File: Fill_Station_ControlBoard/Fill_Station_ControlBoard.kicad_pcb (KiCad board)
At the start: 6 copper layers, 100 x 100 mm, 251 parts, among them IC1 TPS259573DSGR, J1 RJ45_Wuerth_74980111211, J10 Micro_SD_Card_Det_Hirose_DM3AT, J12 Conn_02x05_Counter_Clockwise, J13 Screw_Terminal_2_P5.00mm, J14 Micro_SD_Card_Det_Hirose_DM3AT, J15 USB_C_Receptacle_USB2.0_14P, J16 DE9_Socket_MountingHoles, J18 Screw_Terminal_3_P3.50mm, J2 Ematch1, J6 Ematch2, J7 Screw_Terminal_3_P3.50mm, J8 Screw_Terminal_3_P3.50mm, J9 Screw_Terminal_6_P3.50mm, Q1 AO3400A, Q2 AO3400A, SW1 RESET, SW2 BOOT, U1 TPS62130, U2 STM32H747IITx, U3 INA3221, U4 TPS62130, U5 DP83825I, U6 TPS2116DRL, U7 USBLC6-2SC6, U8 ISOW1044, Y1 ASV-25.000MHz, Y2 ASV-32.768kHz, Y4 ASV-25.000MHz

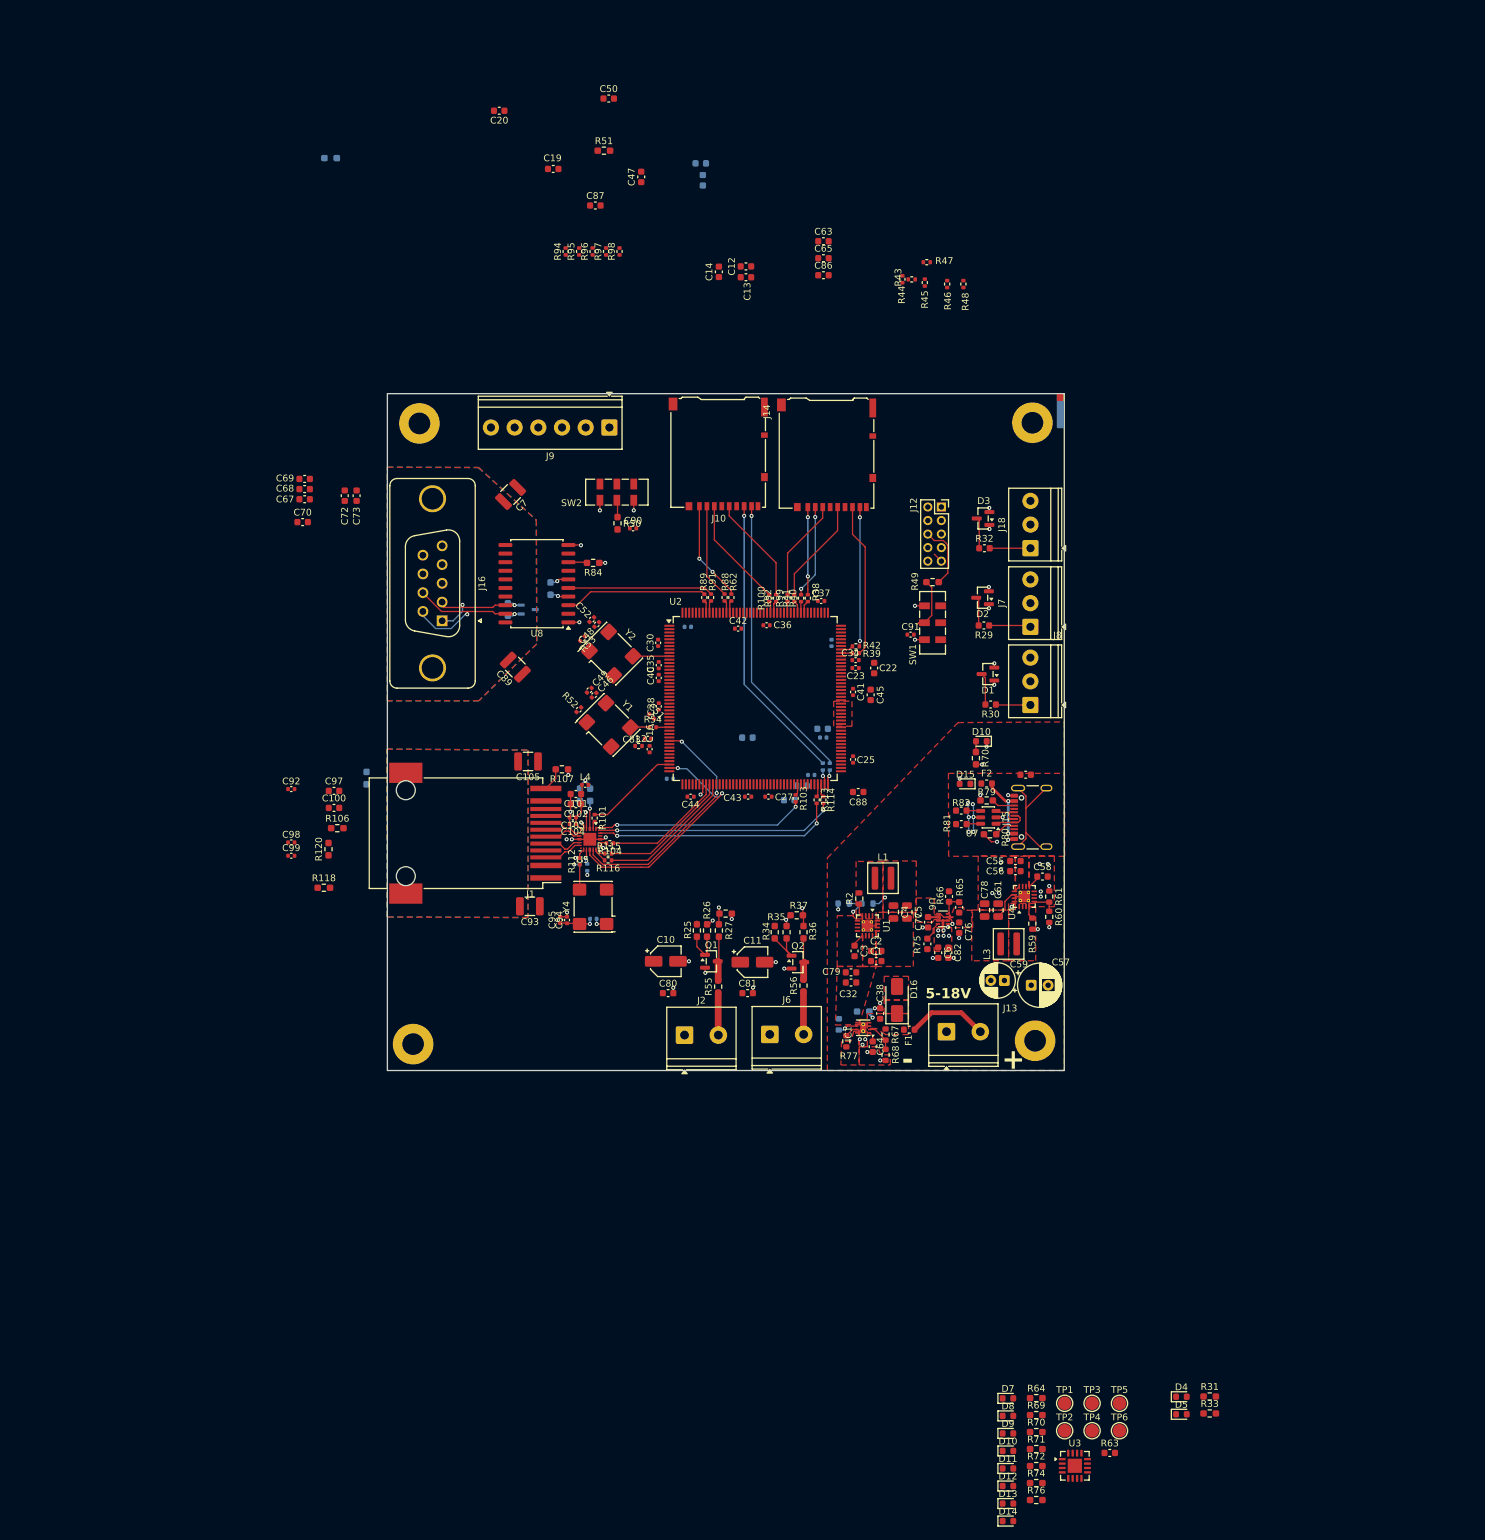
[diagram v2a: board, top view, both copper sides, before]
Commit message: PCB presque terminé
Modifs de l'alim
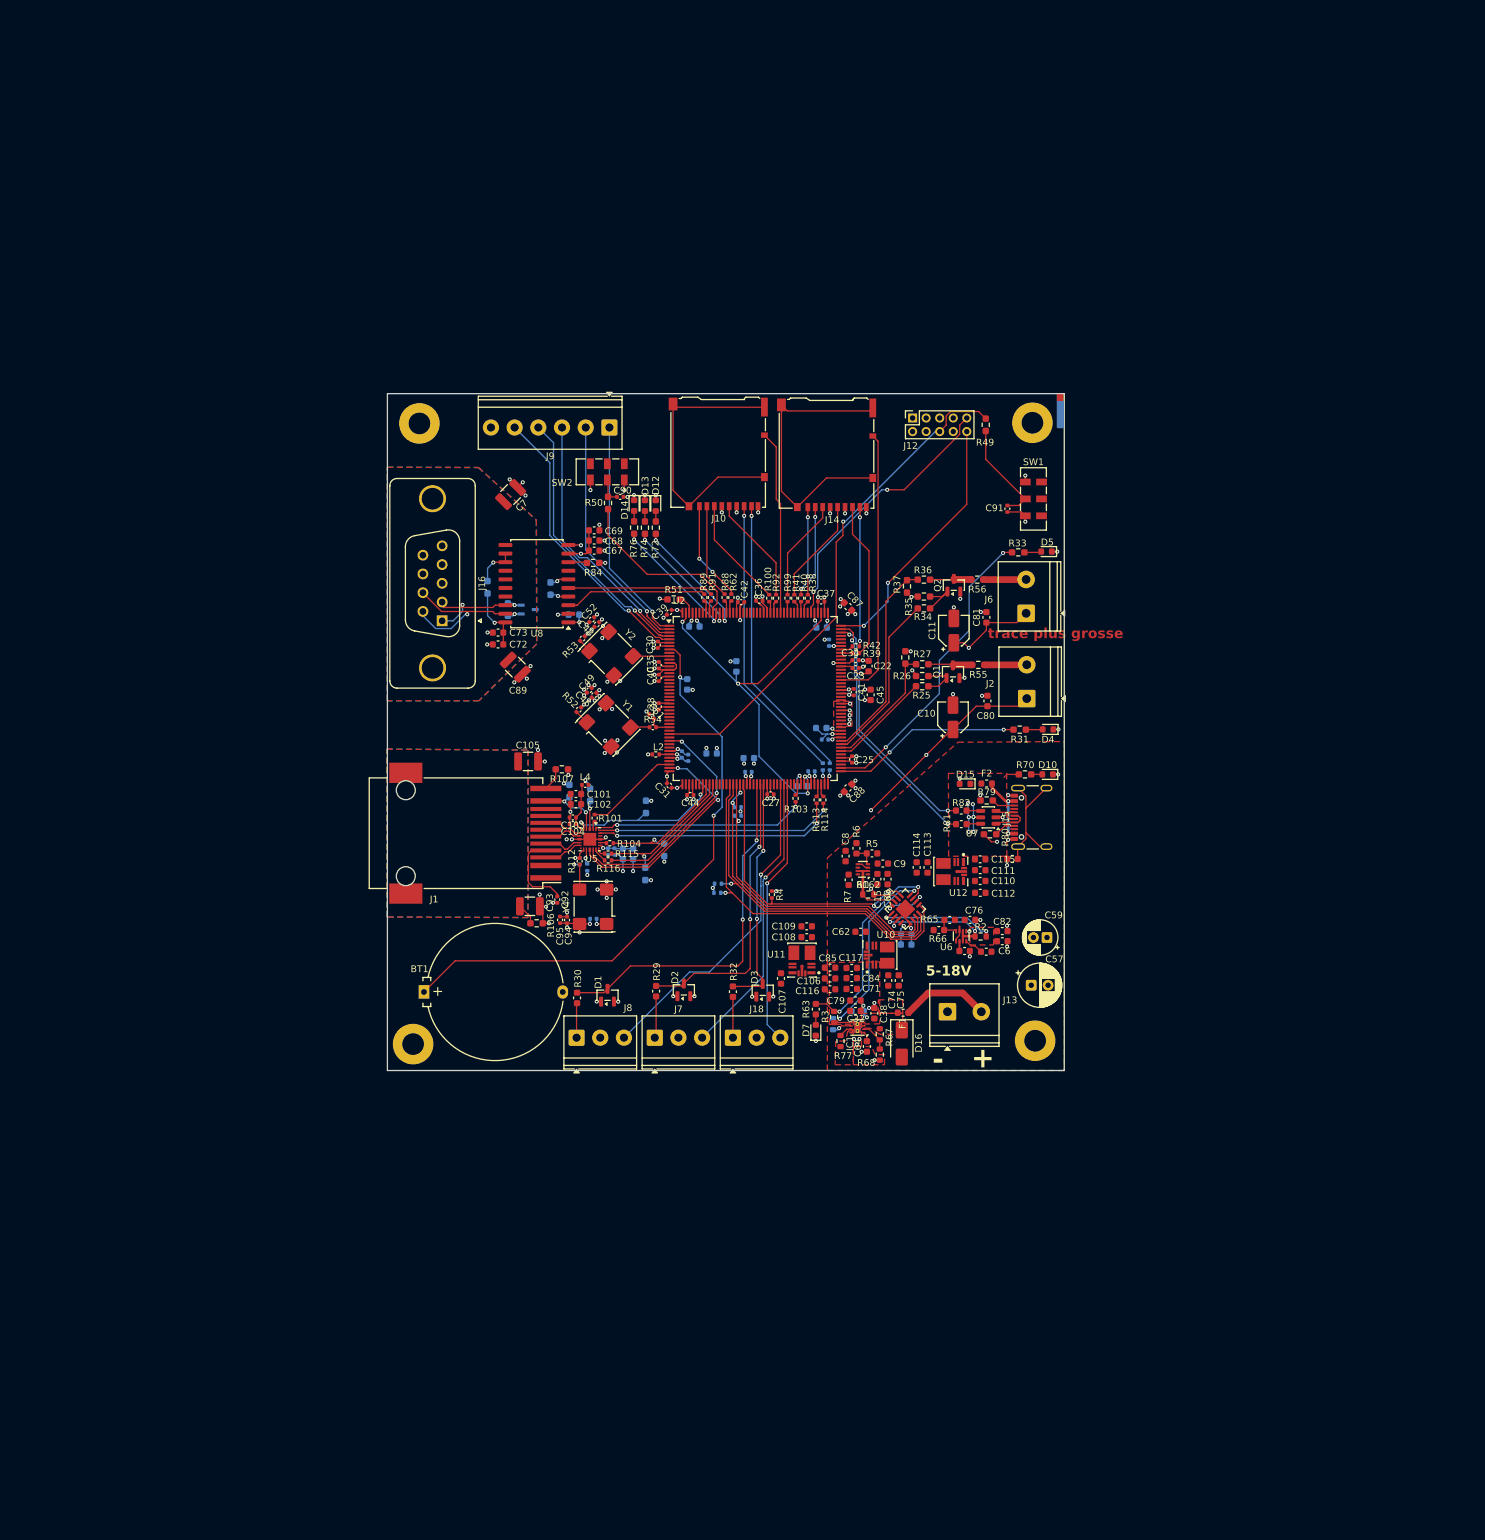
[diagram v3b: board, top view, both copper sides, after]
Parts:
- removed C12, C14, C63, C86: 100n, Capacitor_SMD:C_0603_1608Metric
- removed C13, C55, C65: 10u, Capacitor_SMD:C_0603_1608Metric
- removed C3, C58: 3.3n, Capacitor_SMD:C_0603_1608Metric
- removed C4, C5, C61, C78: 22u, Capacitor_SMD:C_0805_2012Metric
- removed C47, C50: 1u, Capacitor_SMD:C_0603_1608Metric
- removed C56: 0.1u, Capacitor_SMD:C_0603_1608Metric
- removed the D10 at (263.7, 234.2)
- removed D11, D8, D9: LED, LED_SMD:LED_0603_1608Metric
- removed L1, L3: 2.2u, Inductor_SMD:L_Coilcraft_XAL4020-XXX
- removed R43, R44, R45, R46, R47, R48, R94, R95, R96, R97, R98: 10k, Resistor_SMD:R_0402_1005Metric
- removed R59, R60: 100k, Resistor_SMD:R_0603_1608Metric
- removed R61: 316k, Resistor_SMD:R_0603_1608Metric
- removed R64, R69: 1.5k, Resistor_SMD:R_0603_1608Metric_Pad0.98x0.95mm_HandSolder
- removed the R70 at (267.9, 231.4)
- removed R71: 680, Resistor_SMD:R_0603_1608Metric_Pad0.98x0.95mm_HandSolder
- removed TP1, TP2, TP3, TP4, TP5, TP6: TestPoint, TestPoint:TestPoint_Pad_D2.0mm
- removed U3: INA3221, Package_DFN_QFN:Texas_RGV0016A_VQFN-16-1EP_4x4mm_P0.65mm_EP2.1x2.1mm
- removed U4: TPS62130, Package_DFN_QFN:VQFN-16-1EP_3x3mm_P0.5mm_EP1.68x1.68mm_ThermalVias
- added BT1: RTC_BAT, Battery:Battery_Panasonic_CR2032-HFN_Horizontal_CircularHoles, F.Cu at (177.4, 166.4)
- added C106: 10u, Capacitor_SMD:C_0603_1608Metric, F.Cu at (237.4, 164.4)
- added C107: 1u, Capacitor_SMD:C_0603_1608Metric, F.Cu at (230.2, 164.4)
- added C108: 10u, Capacitor_SMD:C_0603_1608Metric, F.Cu at (233.9, 158.3)
- added C109: 22u, Capacitor_SMD:C_0603_1608Metric, F.Cu at (233.9, 156.7)
- added C110: 22u, Capacitor_SMD:C_0603_1608Metric, F.Cu at (259.6, 150.0)
- added C111: 10u, Capacitor_SMD:C_0603_1608Metric, F.Cu at (259.6, 148.4)
- added C112: 1u, Capacitor_SMD:C_0603_1608Metric, F.Cu at (259.6, 151.8)
- added C113: 10u, Capacitor_SMD:C_0603_1608Metric, F.Cu at (251.8, 148.0)
- added C114: 22u, Capacitor_SMD:C_0603_1608Metric, F.Cu at (250.2, 148.0)
- added C115: 100n, Capacitor_SMD:C_0603_1608Metric, F.Cu at (259.6, 146.8)
- added C116: 100n, Capacitor_SMD:C_0603_1608Metric, F.Cu at (237.4, 166.0)
- added C117: 100n, Capacitor_SMD:C_0603_1608Metric, F.Cu at (240.6, 162.8)
- added C15: 10u, Capacitor_SMD:C_0603_1608Metric, F.Cu at (244.4, 149.7)
- added C60: 10u, Capacitor_SMD:C_0603_1608Metric, F.Cu at (245.9, 149.7)
- added C62: 1u, Capacitor_SMD:C_0603_1608Metric, F.Cu at (241.9, 157.5)
- added C71: 10u, Capacitor_SMD:C_0603_1608Metric, F.Cu at (240.6, 165.9)
- added C74: 10u, Capacitor_SMD:C_0603_1608Metric, F.Cu at (246.0, 164.7)
- added C75: 22u, Capacitor_SMD:C_0603_1608Metric, F.Cu at (247.6, 164.7)
- added C8: 1u, Capacitor_SMD:C_0603_1608Metric, F.Cu at (239.7, 146.3)
- added C84: 22u, Capacitor_SMD:C_0603_1608Metric, F.Cu at (240.6, 164.3)
- added C85: 22u, Capacitor_SMD:C_0603_1608Metric, F.Cu at (237.4, 162.8)
- added C9: 1u, Capacitor_SMD:C_0603_1608Metric, F.Cu at (245.2, 147.4)
- added R132: 10k, Resistor_SMD:R_0402_1005Metric, B.Cu at (248.3, 153.6)
- added R133: 10k, Resistor_SMD:R_0402_1005Metric, B.Cu at (220.8, 151.8)
- added R134: 10k, Resistor_SMD:R_0402_1005Metric, B.Cu at (220.8, 150.4)
- added R162: 50m, Resistor_SMD:R_0603_1608Metric, F.Cu at (243.1, 152.0)
- added R5: 365k, Capacitor_SMD:C_0603_1608Metric, F.Cu at (243.6, 145.9)
- added R6: 100k, Capacitor_SMD:C_0603_1608Metric, F.Cu at (241.3, 145.2)
- added R7: 10k, Capacitor_SMD:C_0603_1608Metric, F.Cu at (240.2, 149.8)
- added R8: 10k, Resistor_SMD:R_0402_1005Metric, B.Cu at (223.8, 139.1)
- added R9: 10k, Resistor_SMD:R_0402_1005Metric, B.Cu at (223.8, 140.3)
- added U10: TPSM33620-Q1, TPSM365:RDN0011A-MFG, F.Cu at (244.9, 160.9)
- added U11: TPSM33620-Q1, TPSM365:RDN0011A-MFG, F.Cu at (233.2, 161.6)
- added U12: TPSM33620-Q1, TPSM365:RDN0011A-MFG, F.Cu at (255.2, 148.6)
- added U9: TPS2116DRL, Package_TO_SOT_SMD:SOT-583-8, F.Cu at (242.2, 148.3)
- C1: value 10u -> 100n; moved to B.Cu
- C100, C16, C19, C20, C43, C70, C83, C97, C98, C99, R118, R120: moved to B.Cu
- C2: value 0.1u -> 10u; moved to B.Cu
- C31, C39: moved to F.Cu
- R2: value 100k -> 50m
- R3: value 100k -> 50m; moved to F.Cu
- R4: value 316k -> 10k; footprint Resistor_SMD:R_0603_1608Metric -> Resistor_SMD:R_0402_1005Metric; moved to F.Cu
- U1: value TPS62130 -> INA3221; footprint Package_DFN_QFN:VQFN-16-1EP_3x3mm_P0.5mm_EP1.68x1.68mm_ThermalVias -> Package_DFN_QFN:Texas_RGV0016A_VQFN-16-1EP_4x4mm_P0.65mm_EP2.1x2.1mm
- moved D14 159.9 mm to (208.4, 94.5), turned to -90 degrees
- moved D13 156.9 mm to (210.1, 94.5), turned to -90 degrees
- moved R76 155.5 mm to (208.4, 97.8), turned to -90 degrees
- moved D12 153.9 mm to (211.7, 94.5), turned to -90 degrees
- moved R74 152.5 mm to (210.1, 97.8), turned to -90 degrees
- moved R72 149.6 mm to (211.7, 97.8), turned to -90 degrees
- moved R33 130.3 mm to (265.2, 101.5), turned to 180 degrees
- moved D5 129.0 mm to (269.4, 101.3), turned to 180 degrees
- moved R31 102.4 mm to (265.4, 127.6), turned to 180 degrees
- moved D4 100.6 mm to (269.6, 127.6), turned to 180 degrees
- moved C20 89.2 mm to (216.3, 121.0), turned to -90 degrees
- moved J18 84.6 mm to (223.1, 173.2), turned to 0 degrees
- moved J8 83.1 mm to (200.0, 173.2), turned to 0 degrees
- moved J7 82.2 mm to (211.5, 173.2), turned to 0 degrees
- moved R63 78.6 mm to (235.3, 168.9), turned to 90 degrees
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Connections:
- net /Ethernet/TXEN renamed /Ethernet/Eth.TXEN
- C1 pad 1: 12.8V -> 3V3
- C2 pad 1: 12.8V -> GND
- C2 pad 2: GND -> 3V3
- IC1 pad 5: 12.8V -> /Alimentation/Psense1_IN+
- R2 pad 1: Net-(U1-PG) -> /Alimentation/Psense3_IN+
- R2 pad 2: 3V3_Bat -> 3V3
- R3 pad 1: Net-(U1-FB) -> /Alimentation/Psense1_IN+
- R3 pad 2: 3V3_Bat -> 12.8V
- R4 pad 1: GND -> 3V3
- R4 pad 2: Net-(U1-FB) -> /Alimentation/PM_TC
- R63 pad 2: 12.8V_BAT -> 12.8V
- R72 pad 2: /Monitor/LED1 -> /Alimentation/LED1
- R73 pad 2: 12.8V -> /Alimentation/Psense1_IN+
- R74 pad 2: /Monitor/LED2 -> /Alimentation/LED2
- R76 pad 2: /Monitor/LED3 -> /Alimentation/LED3
- U1 pad 1: /Alimentation/3V3_SW -> 3V3
- U1 pad 10: 12.8V -> Net-(U1-PV)
- U1 pad 12: 12.8V -> /Alimentation/Psense1_IN+
- U1 pad 13: 12.8V -> /Alimentation/PM_TC
- U1 pad 14: 3V3_Bat -> 5V
- U1 pad 15: GND -> /Alimentation/Psense2_IN+
- U1 pad 16: GND -> Net-(U1-VPU)
- U1 pad 2: /Alimentation/3V3_SW -> /Alimentation/Psense3_IN+
- U1 pad 3: /Alimentation/3V3_SW -> GND
- U1 pad 4: Net-(U1-PG) -> 3V3
- U1 pad 5: Net-(U1-FB) -> GND
- U1 pad 6: GND -> /Alimentation/PM_SCL
- U1 pad 7: GND -> /Alimentation/PM_SDA
- U1 pad 8: GND -> /Alimentation/PM_WARN
- U1 pad 9: Net-(U1-SS/TR) -> /Alimentation/PM_CRIT
- U2 pad 1: unconnected-(U2-PE2-Pad1) -> /Control/GPIO1
- U2 pad 146: /MCU/LED1 -> unconnected-(U2-PD3-Pad146)
- U2 pad 147: /MCU/LED2 -> /MCU/SD2.DET
- U2 pad 148: /MCU/LED3 -> unconnected-(U2-PD5-Pad148)
- U2 pad 164: unconnected-(U2-PB5-Pad164) -> /Alimentation/LED1
- U2 pad 165: unconnected-(U2-PB6-Pad165) -> /Alimentation/LED2
- U2 pad 166: unconnected-(U2-PB7-Pad166) -> /Alimentation/LED3
- U2 pad 2: /Control/Heater1 -> /Control/GPIO2
- U2 pad 3: /Control/Heater2 -> /Control/GPIO3
- U2 pad 4: /Control/Heater3 -> /Control/GPIO4
- U2 pad 5: unconnected-(U2-PE6-Pad5) -> /Control/GPIO5
- U2 pad 59: unconnected-(U2-PF12-Pad59) -> /Alimentation/PM_CRIT
- U2 pad 60: unconnected-(U2-PF13-Pad60) -> /Alimentation/PM_WARN
- U2 pad 61: unconnected-(U2-PF14-Pad61) -> /Alimentation/PM_SCL
- U2 pad 62: unconnected-(U2-PF15-Pad62) -> /Alimentation/PM_SDA
- U2 pad 63: unconnected-(U2-PG0-Pad63) -> /Alimentation/PM_TC
- U2 pad 67: /Control/Servo.Signal1 -> /Control/Servo.Signal3
- U2 pad 69: /Control/Servo.Signal3 -> /Control/Servo.Signal1
- U2 pad 72: /Control/GPIO1 -> unconnected-(U2-PE10-Pad72)
- U2 pad 73: /Control/GPIO2 -> unconnected-(U2-PE11-Pad73)
- U2 pad 74: /Control/GPIO3 -> /Control/Heater3
- U2 pad 75: /Control/GPIO4 -> /Control/Heater2
- U2 pad 76: /Control/GPIO5 -> /Control/Heater1
- U2 pad 77: /Control/GPIO6 -> unconnected-(U2-PE15-Pad77)
- U2 pad 95: /Control/E-match2_Det -> /Control/E-match1
- U2 pad 96: /Control/E-match2 -> /Control/E-match1_Det
- U2 pad 97: /Control/E-match1_Det -> /Control/E-match2
- U2 pad 98: /Control/E-match1 -> /Control/E-match2_Det
- U6 pad 2: 3V3 -> /Alimentation/Psense3_IN+
- U6 pad 7: 3V3 -> /Alimentation/Psense3_IN+
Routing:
- net GND: track 50.3 -> 185.5 mm, vias 54 -> 132
- net 12.8V: track 0.00 -> 124.7 mm, vias 0 -> 5
- net 5V: track 0.00 -> 112.1 mm, vias 0 -> 3
- net 3V3: track 21.5 -> 108.8 mm, vias 16 -> 61
- net Net-(U2-VBAT): track 0.00 -> 87.3 mm, vias 0 -> 2
- net /MCU/NRST: track 9.67 -> 75.4 mm, vias 0 -> 1
- net Net-(C24-Pad1): track 0.00 -> 56.0 mm, vias 0 -> 3
- net /Alimentation/PM_CRIT: track 0.00 -> 54.1 mm, vias 0 -> 1
- net /Alimentation/PM_WARN: track 0.00 -> 51.3 mm, vias 0 -> 1
- net /Control/Heater3: track 0.00 -> 48.7 mm, vias 0 -> 1
- net /Control/Servo.Signal3: track 4.73 -> 53.4 mm, vias 0 -> 2
- net /Alimentation/PM_SDA: track 0.00 -> 48.1 mm, vias 0 -> 2
- net /Alimentation/PM_SCL: track 0.00 -> 46.6 mm, vias 0 -> 1
- net /Control/E-match2_Cont: track 0.00 -> 45.1 mm, vias 0 -> 2
- net Net-(J14-SHIELD): track 0.00 -> 43.1 mm
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- added copper zone on In3.Cu, net GND
- removed copper zone on F.Cu, net /Alimentation/3V3_SW
- removed copper zone on F.Cu, net /Alimentation/3V3_SW_USB
- removed copper zone on F.Cu, net 3V3_Bat
- removed copper zone on F.Cu, net 3V3_USB
- removed copper zone on In3.Cu, net 5V
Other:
- board text added: "3V3_BAT"
- board text added: "3V3_Bus"
- board text added: "3V3_USB"
- board text added: "5V_BAT"
- board text added: "5V_Bus"
- board text added: "E-Fuse"
- board text added: "trace plus grosse"

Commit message: finalisé le pcb
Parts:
- added BZ1: Buzzer_TDK_PS1240, Buzzer_Beeper:Buzzer_Murata_PKMCS0909E, F.Cu at (218.2, 157.6)
- added C12: 100n, Capacitor_SMD:C_0603_1608Metric, B.Cu at (238.4, 94.7)
- added C13: 10u, Capacitor_SMD:C_0603_1608Metric, B.Cu at (238.4, 93.1)
- added C14: 100n, Capacitor_SMD:C_0603_1608Metric, F.Cu at (246.3, 80.0)
- added C47: 1u, Capacitor_SMD:C_0603_1608Metric, F.Cu at (229.0, 139.7)
- added C50: 1u, Capacitor_SMD:C_0603_1608Metric, F.Cu at (210.5, 122.2)
- added C63: 100n, Capacitor_SMD:C_0603_1608Metric, B.Cu at (222.5, 96.6)
- added C65: 10u, Capacitor_SMD:C_0603_1608Metric, B.Cu at (222.5, 98.2)
- added C86: 100n, Capacitor_SMD:C_0603_1608Metric, F.Cu at (211.0, 79.5)
- added D11: LED, LED_SMD:LED_0603_1608Metric, F.Cu at (244.6, 144.7)
- added D8: LED, LED_SMD:LED_0603_1608Metric, F.Cu at (271.1, 142.4)
- added D9: LED, LED_SMD:LED_0603_1608Metric, F.Cu at (270.9, 153.7)
- added R10: 1k, Resistor_SMD:R_0603_1608Metric, F.Cu at (211.0, 160.2)
- added R11: 1k, Resistor_SMD:R_0603_1608Metric, F.Cu at (218.2, 152.0)
- added R43: 10k, Resistor_SMD:R_0402_1005Metric, F.Cu at (233.2, 96.9)
- added R44: 10k, Resistor_SMD:R_0402_1005Metric, F.Cu at (234.6, 97.6)
- added R45: 10k, Resistor_SMD:R_0402_1005Metric, F.Cu at (237.1, 97.2)
- added R46: 10k, Resistor_SMD:R_0402_1005Metric, F.Cu at (240.3, 98.9)
- added R47: 10k, Resistor_SMD:R_0402_1005Metric, F.Cu at (242.6, 97.5)
- added R48: 10k, Resistor_SMD:R_0402_1005Metric, F.Cu at (246.0, 84.8)
- added R64: 1.5k, Resistor_SMD:R_0603_1608Metric_Pad0.98x0.95mm_HandSolder, F.Cu at (271.1, 145.6)
- added R69: 1.5k, Resistor_SMD:R_0603_1608Metric_Pad0.98x0.95mm_HandSolder, F.Cu at (270.9, 157.0)
- added R71: 680, Resistor_SMD:R_0603_1608Metric_Pad0.98x0.95mm_HandSolder, F.Cu at (244.6, 147.9)
- added R94: 10k, Resistor_SMD:R_0402_1005Metric, F.Cu at (217.3, 97.4)
- added R95: 10k, Resistor_SMD:R_0402_1005Metric, F.Cu at (219.8, 100.8)
- added R96: 10k, Resistor_SMD:R_0402_1005Metric, F.Cu at (220.9, 97.4)
- added R97: 10k, Resistor_SMD:R_0402_1005Metric, F.Cu at (225.2, 97.3)
- added R98: 10k, Resistor_SMD:R_0402_1005Metric, F.Cu at (226.5, 97.3)
- added TP1: TestPoint, TestPoint:TestPoint_Pad_D2.0mm, B.Cu at (270.0, 157.0)
- added TP2: TestPoint, TestPoint:TestPoint_Pad_D2.0mm, B.Cu at (270.0, 153.0)
- added TP3: TestPoint, TestPoint:TestPoint_Pad_D2.0mm, B.Cu at (270.0, 149.0)
- added TP4: TestPoint, TestPoint:TestPoint_Pad_D2.0mm, B.Cu at (270.0, 161.0)
- C1, C2, R78: moved to F.Cu
- R6: footprint Capacitor_SMD:C_0603_1608Metric -> Resistor_SMD:R_0603_1608Metric
- moved D7 35.7 mm to (270.8, 167.9)
- moved R63 35.7 mm to (270.8, 164.8)
- moved C109 34.9 mm to (268.8, 157.3), turned to 90 degrees
- moved C108 33.3 mm to (267.2, 157.3), turned to 90 degrees
- moved C107 31.3 mm to (260.3, 155.9)
- moved U11 31.1 mm to (263.9, 156.6), turned to 90 degrees
- moved R7 29.7 mm to (269.5, 145.6)
- moved C59 26.1 mm to (248.2, 173.5), turned to 0 degrees
- moved C116 25.8 mm to (262.7, 160.7), turned to -90 degrees
- moved R162 25.3 mm to (267.5, 145.6), turned to -90 degrees
- moved C106 24.0 mm to (261.1, 160.7), turned to -90 degrees
- moved R77 23.7 mm to (262.0, 168.1)
- moved C15 23.3 mm to (267.7, 148.8)
- moved C60 23.3 mm to (269.2, 148.8)
- moved U9 22.8 mm to (264.8, 144.7), turned to -90 degrees
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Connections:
- C24 pad 1: Net-(C24-Pad1) -> 3V3
- C57 pad 1: 12.8V_BAT -> VIN
- C59 pad 1: 12.8V_BAT -> VIN
- F1 pad 1: Net-(F1-Pad1) -> VIN
- J13 pad 2: Net-(F1-Pad1) -> VIN
- R81 pad 1: /MCU/USBC.DP -> /MCU/USBC.DM
- R82 pad 2: /MCU/USBC.DM -> /MCU/USBC.DP
- U2 pad 135: Net-(C24-Pad1) -> 3V3
- U2 pad 175: Net-(C24-Pad1) -> 3V3
- U2 pad 82: Net-(C24-Pad1) -> 3V3
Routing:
- net 3V3: track 108.8 -> 201.1 mm, vias 61 -> 74
- net GND: track 185.5 -> 247.1 mm, vias 132 -> 167
- net 12.8V: track 124.7 -> 66.5 mm, vias 5 -> 21
- net Net-(C24-Pad1): track 56.0 -> 0.00 mm, vias 3 -> 0
- net 5V: track 112.1 -> 161.4 mm, vias 3 -> 4
- net /Alimentation/Psense2_IN+: track 12.4 -> 37.7 mm
- net 5V_USB: track 14.3 -> 37.7 mm
- net /Alimentation/PM_CRIT: track 54.1 -> 31.9 mm
- net /Alimentation/PM_WARN: track 51.3 -> 31.5 mm
- net /Alimentation/PM_SDA: track 48.1 -> 30.1 mm
- net /Alimentation/PM_SCL: track 46.6 -> 30.2 mm
- net Net-(F1-Pad1): track 13.1 -> 0.00 mm
- net /Control/E-match1: track 15.1 -> 26.3 mm, vias 0 -> 2
- net /MCU/USBC.DP: track 37.4 -> 26.2 mm, vias 2 -> 0
- net /Control/E-match2: track 25.3 -> 36.3 mm, vias 0 -> 2
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- added copper zone on In3.Cu, net 12.8V
- added copper zone on F.Cu, net 3V3_Bat
- added copper zone on In3.Cu, net 3V3_Bat
- added copper zone on F.Cu, net 3V3_USB
- added copper zone on F.Cu, net 5V_Bat
- added copper zone on In3.Cu, net 5V_Bat
- added copper zone on F.Cu, net VIN
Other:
- board text added: "BOOT"
- board text added: "CAN FD w/ termination"
- board text added: "E-Match 1"
- board text added: "E-Match 2"
- board text added: "GND"
- board text added: "H"
- board text added: "RESET"
- board text added: "SD1"
- board text added: "SWCLK"
- board text added: "SWDIO"
- board text added: "Servo1"
- board text added: "Servo2"
- board text added: "Servo3"
- board text added: "Sig"
- board text removed: "Pas de fil icite"
- board text removed: "trace plus grosse"
